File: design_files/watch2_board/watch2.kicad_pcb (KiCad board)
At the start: 16 copper layers, 43.7 x 35.6 mm, 8 parts, among them U1 ESP32-WROVER

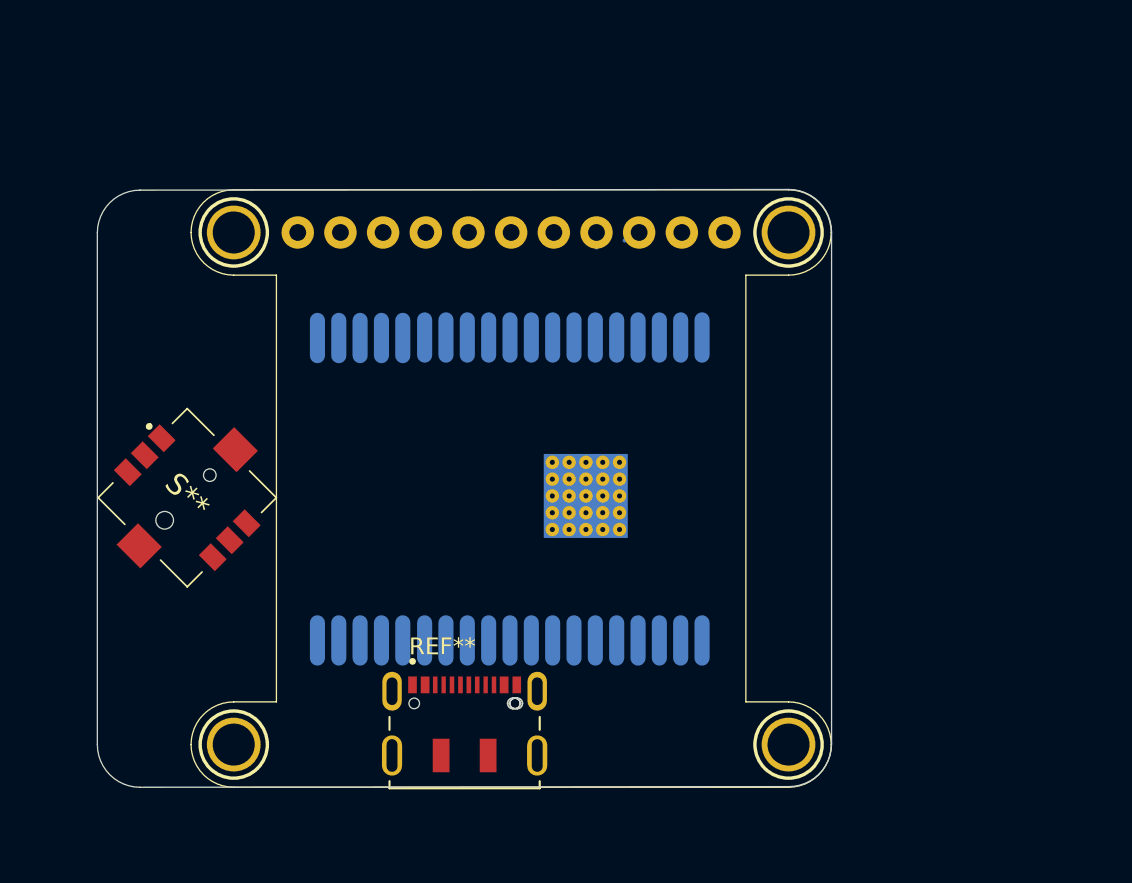
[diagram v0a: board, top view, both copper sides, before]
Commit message: added torch + ir stuff to schematic and did some pcb stuff
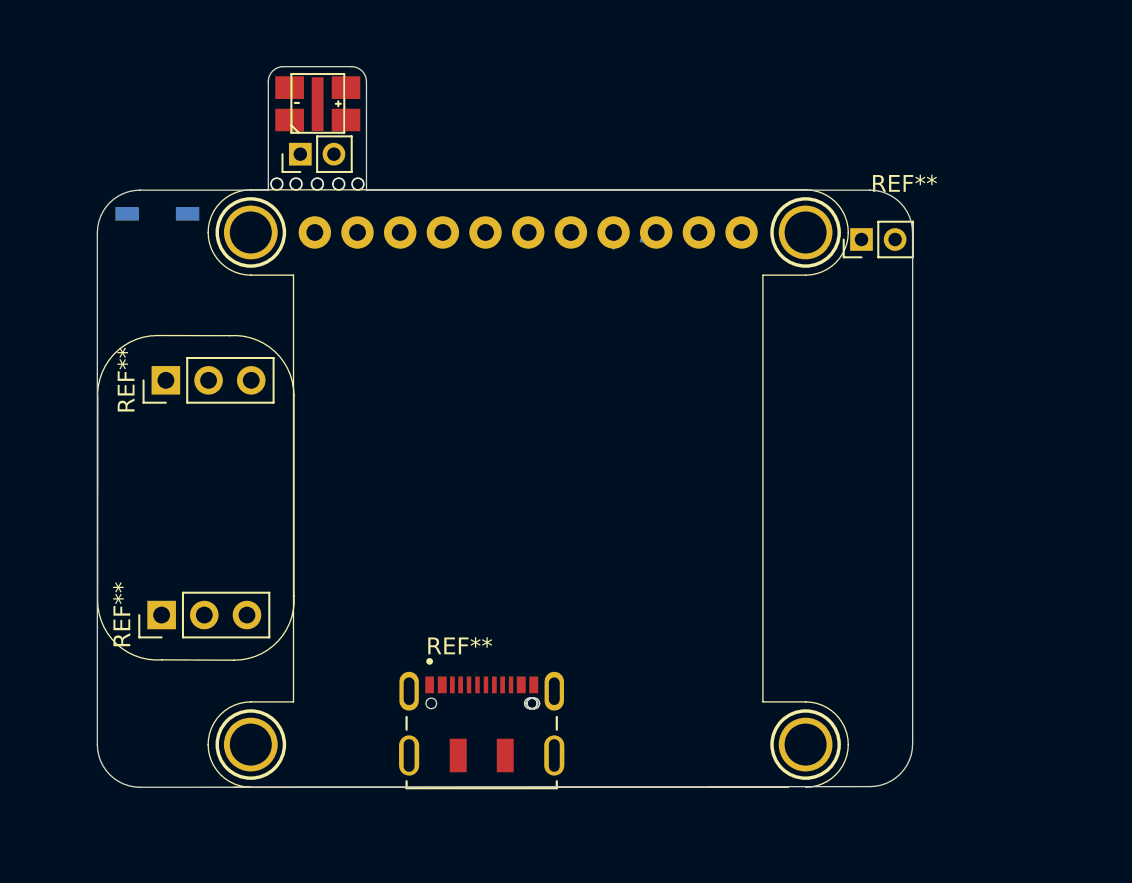
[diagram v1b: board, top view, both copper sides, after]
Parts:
- removed S**: SKRHABE010, Alice's Library:SKRHABE010
- removed U1: ESP32-WROVER, Alice's Library:ESP32-WROVER
- added IR LED: SOD4223X290N, Alice's Library:SOD4223X290N, B.Cu at (131.6, 86.6)
- added REF**: PinHeader_1x03_P2.54mm_Vertical, Connector_PinHeader_2.54mm:PinHeader_1x03_P2.54mm_Vertical, F.Cu at (132.1, 96.5)
- added REF**: PinHeader_1x03_P2.54mm_Vertical, Connector_PinHeader_2.54mm:PinHeader_1x03_P2.54mm_Vertical, F.Cu at (131.8, 110.5)
- added REF**: PinHeader_1x02_P2.00mm_Vertical, Connector_PinHeader_2.00mm:PinHeader_1x02_P2.00mm_Vertical, F.Cu at (140.1, 83.1)
- added REF**: PinHeader_1x02_P2.00mm_Vertical, Connector_PinHeader_2.00mm:PinHeader_1x02_P2.00mm_Vertical, F.Cu at (173.5, 88.1)
- added REF**: MLCAWT-A1-0000-000XE1, Alice's Library:MLCAWT-A1-0000-000XE1, F.Cu at (141.1, 80.1)
- moved U$7 1.02 mm to (137.1, 118.2)
- moved U$9 1.02 mm to (137.1, 87.7)
- moved JP1 1.02 mm to (153.6, 87.7)
- moved REF** 1.02 mm to (150.9, 115.7)
- moved U$10 1.02 mm to (170.2, 87.7)
- moved U$8 1.02 mm to (170.2, 118.2)
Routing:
- net (no net): vias 0 -> 5
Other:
- board size 43.7 x 35.6 mm -> 48.5 x 42.9 mm

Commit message: created watch2 pcb it's mostly populated and wired up.  i haven't checked it yet, and i haven't figured out how to make IO0 externaly pressable yet :)
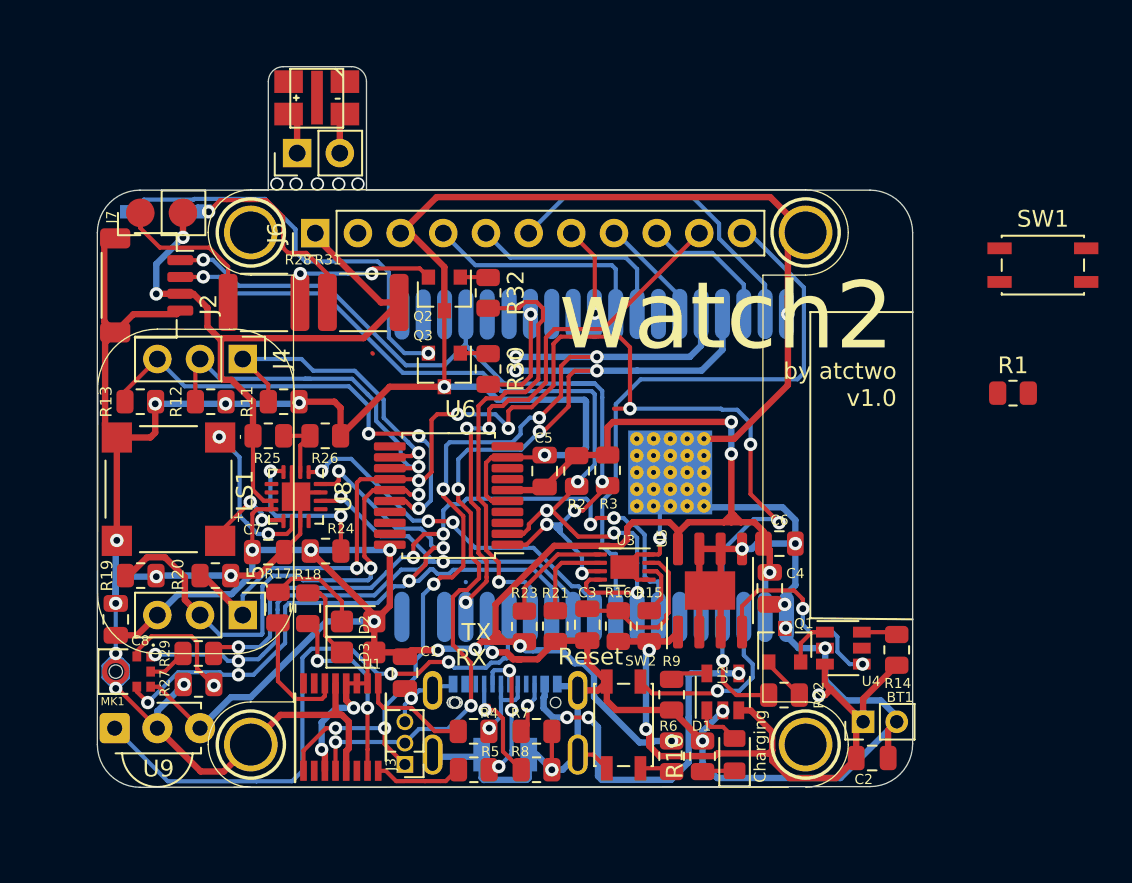
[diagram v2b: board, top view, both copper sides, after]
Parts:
- removed IR LED: SOD4223X290N, Alice's Library:SOD4223X290N
- removed JP1: , 1X11_ROUND_76
- removed REF** (x2): PinHeader_1x03_P2.54mm_Vertical, Connector_PinHeader_2.54mm:PinHeader_1x03_P2.54mm_Vertical
- removed REF** (x2): PinHeader_1x02_P2.00mm_Vertical, Connector_PinHeader_2.00mm:PinHeader_1x02_P2.00mm_Vertical
- removed REF**: MLCAWT-A1-0000-000XE1, Alice's Library:MLCAWT-A1-0000-000XE1
- removed REF**: JAE_DX07S016JA1R1500, Alice's Library:JAE_DX07S016JA1R1500
- added BT1: Battery_Cell, Connector_PinHeader_2.00mm:PinHeader_1x02_P2.00mm_Vertical, F.Cu at (173.6, 116.8)
- added C1: 0.1uF, Capacitor_SMD:C_0805_2012Metric, F.Cu at (146.3, 113.9)
- added C2: 10uF, Capacitor_SMD:C_0805_2012Metric, F.Cu at (174.1, 119.0)
- added C3: 10nF, Capacitor_SMD:C_0805_2012Metric, F.Cu at (157.2, 111.1)
- added C4: 10uF, Capacitor_SMD:C_0805_2012Metric, F.Cu at (168.0, 108.9)
- added C5: 0.1uF, Capacitor_SMD:C_0805_2012Metric, F.Cu at (154.6, 101.9)
- added C6: 0.1uF, Capacitor_SMD:C_0805_2012Metric, F.Cu at (168.6, 106.2)
- added C7: 0.1uF, Capacitor_SMD:C_0805_2012Metric, F.Cu at (138.2, 106.7)
- added C8: 0.1uF, Capacitor_SMD:C_0805_2012Metric, F.Cu at (129.1, 110.7)
- added D1: LED, LED_SMD:LED_0805_2012Metric_Castellated, F.Cu at (165.9, 118.8)
- added D2: TX, LED_SMD:LED_0805_2012Metric_Castellated, F.Cu at (143.5, 110.9)
- added D3: RX, LED_SMD:LED_0805_2012Metric_Castellated, F.Cu at (143.5, 112.7)
- added D4: LED_TORCH, Alice's Library:MLCAWT-A1-0000-000XE1, F.Cu at (141.1, 79.7)
- added D5: LED_IR, Alice's Library:SOD4223X290N, B.Cu at (131.8, 86.5)
- added J1: USB_C_Receptacle_USB2.0, Alice's Library:JAE_DX07S016JA1R1500, B.Cu at (152.3, 115.7)
- added J2: STEMMA QT, Connector_JST:JST_SH_SM04B-SRSS-TB_1x04-1MP_P1.00mm_Horizontal, F.Cu at (130.9, 90.9)
- added J3: UART Connector, Connector_PinHeader_1.27mm:PinHeader_1x03_P1.27mm_Vertical, F.Cu at (146.3, 119.4)
- added J4: Conn_01x03_Male, Connector_PinHeader_2.54mm:PinHeader_1x03_P2.54mm_Vertical, F.Cu at (136.7, 95.2)
- added J5: Conn_01x03_Male, Connector_PinHeader_2.54mm:PinHeader_1x03_P2.54mm_Vertical, F.Cu at (136.7, 110.5)
- added J6: TFT Connector, Connector_PinHeader_2.54mm:PinHeader_1x11_P2.54mm_Vertical, F.Cu at (141.0, 87.8)
- added J7: Torch Connector (main board), Connector_PinHeader_2.54mm:PinHeader_1x02_P2.54mm_Vertical, F.Cu at (130.6, 86.6)
- added J8: Torch Connector (daughter board), Connector_PinHeader_2.54mm:PinHeader_1x02_P2.54mm_Vertical, F.Cu at (139.9, 83.0)
- added LS1: Speaker, Alice's Library:XDCR_CMT-7525-80-SMT-TR, F.Cu at (132.2, 103.0)
- added MK1: SPH0645LM4H-B, Alice's Library:MIC_SPH0645LM4H-B, F.Cu at (129.1, 113.9)
- added Q1: Q_NPN_BCE, Package_TO_SOT_SMD:SOT-23, F.Cu at (168.9, 112.3)
- added Q2: Q_NPN_BCE, Package_TO_SOT_SMD:SOT-23, F.Cu at (148.7, 91.4)
- added Q3: Q_NPN_BCE, Package_TO_SOT_SMD:SOT-23, F.Cu at (148.7, 95.9)
- added R1: 1k, Resistor_SMD:R_0805_2012Metric, F.Cu at (182.5, 97.3)
- added R10: 1k, Resistor_SMD:R_0805_2012Metric, F.Cu at (164.0, 118.9)
- added R11: R, Resistor_SMD:R_0805_2012Metric, F.Cu at (139.1, 97.8)
- added R12: R, Resistor_SMD:R_0805_2012Metric, F.Cu at (134.7, 97.8)
- added R13: R, Resistor_SMD:R_0805_2012Metric, F.Cu at (130.6, 97.8)
- added R14: 1k, Resistor_SMD:R_0805_2012Metric, F.Cu at (175.6, 112.6)
- added R15: 1k, Resistor_SMD:R_0805_2012Metric, F.Cu at (160.8, 111.1)
- added R16: 180R, Resistor_SMD:R_0805_2012Metric, F.Cu at (159.0, 111.1)
- added R17: 1k, Resistor_SMD:R_0805_2012Metric, F.Cu at (138.7, 110.0)
- added R18: 1k, Resistor_SMD:R_0805_2012Metric, F.Cu at (140.5, 110.1)
- added R19: R, Resistor_SMD:R_0805_2012Metric, F.Cu at (130.6, 108.1)
- added R2: 4k7, Resistor_SMD:R_0805_2012Metric, F.Cu at (156.5, 101.9)
- added R20: R, Resistor_SMD:R_0805_2012Metric, F.Cu at (135.0, 108.1)
- added R21: 4k1, Resistor_SMD:R_0805_2012Metric, F.Cu at (155.3, 111.1)
- added R22: 1k, Resistor_SMD:R_0805_2012Metric, F.Cu at (168.9, 115.3)
- added R23: 4k7, Resistor_SMD:R_0805_2012Metric, F.Cu at (153.4, 111.2)
- added R24: 680k, Resistor_SMD:R_0805_2012Metric, F.Cu at (141.6, 106.7)
- added R25: 100k, Resistor_SMD:R_0805_2012Metric, F.Cu at (138.2, 99.8)
- added R26: 100k, Resistor_SMD:R_0805_2012Metric, F.Cu at (141.6, 99.8)
- added R27: 10k, Resistor_SMD:R_0805_2012Metric, F.Cu at (134.0, 114.6)
- added R28: 100R, Resistor_SMD:R_1812_4532Metric, F.Cu at (137.9, 91.9)
- added R29: 68R, Resistor_SMD:R_0805_2012Metric, F.Cu at (134.0, 112.8)
- added R3: 4k7, Resistor_SMD:R_0805_2012Metric, F.Cu at (158.4, 101.9)
- added R30: 1k, Resistor_SMD:R_0805_2012Metric, F.Cu at (151.3, 95.8)
- added R31: 100R, Resistor_SMD:R_1812_4532Metric, F.Cu at (143.8, 91.9)
- added R32: 1k, Resistor_SMD:R_0805_2012Metric, F.Cu at (151.3, 91.3)
- added R4: 27R, Resistor_SMD:R_0805_2012Metric, F.Cu at (150.4, 117.4)
- added R5: 27R, Resistor_SMD:R_0805_2012Metric, F.Cu at (150.4, 119.7)
- added R6: 1k, Resistor_SMD:R_0805_2012Metric, F.Cu at (162.2, 118.9)
- added R7: 5k1, Resistor_SMD:R_0805_2012Metric, F.Cu at (154.1, 117.4)
- added R8: 5k1, Resistor_SMD:R_0805_2012Metric, F.Cu at (154.1, 119.7)
- added R9: 2k, Resistor_SMD:R_0805_2012Metric, F.Cu at (162.2, 115.2)
- added SW1: SW_Push, Button_Switch_SMD:SW_SPST_EVQP2, F.Cu at (184.3, 89.7)
- added SW2: SW_Push, Button_Switch_SMD:SW_SPST_EVQP2, F.Cu at (159.3, 117.0)
- added U1: FT230XS, Package_SO:SSOP-16_3.9x4.9mm_P0.635mm, F.Cu at (142.5, 117.2)
- added U2: MCP73831-2-OT, Package_TO_SOT_SMD:SOT-23-5, F.Cu at (165.2, 115.1)
- added U3: MAX17043G+U, Package_DFN_QFN:DFN-8-1EP_3x2mm_P0.5mm_EP1.7x1.4mm, F.Cu at (159.4, 107.6)
- added U4: MAX16150AUT+T, Package_TO_SOT_SMD:SOT-23-6, F.Cu at (172.4, 112.5)
- added U5: MAX604, Package_SO:SOIC-8-1EP_3.9x4.9mm_P1.27mm_EP2.29x3mm, F.Cu at (164.5, 109.0)
- added U6: MCP23008-xSS, Package_SO:SSOP-20_5.3x7.2mm_P0.65mm, F.Cu at (148.9, 103.4)
- added U7: ESP32-WROVER, Alice's Library:ESP32-WROVER, B.Cu at (169.9, 101.6)
- added U8: MAX98357AETE+T, Package_DFN_QFN:QFN-16-1EP_3x3mm_P0.5mm_EP1.7x1.7mm, F.Cu at (139.8, 103.4)
- added U9: TSOP38238, OptoDevice:Vishay_MINICAST-3Pin, F.Cu at (129.0, 117.2)
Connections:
- U$10 pad P$1: (no net) -> GND
- U$7 pad P$1: (no net) -> GND
- U$8 pad P$1: (no net) -> GND
- U$9 pad P$1: (no net) -> GND
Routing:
- net GND: track 0.00 -> 296.1 mm, vias 0 -> 24
- net +3V3: track 0.00 -> 182.4 mm, vias 0 -> 15
- net DPAD_ENTER: track 0.00 -> 76.3 mm, vias 0 -> 8
- net +5V: track 0.00 -> 61.4 mm, vias 0 -> 6
- net ESP_RX: track 0.00 -> 54.6 mm, vias 0 -> 7
- net I2C_SDA: track 0.00 -> 54.0 mm, vias 0 -> 5
- net ESP_TX: track 0.00 -> 53.7 mm, vias 0 -> 6
- net I2C_SCL: track 0.00 -> 53.2 mm, vias 0 -> 5
- net I2S_BLK: track 0.00 -> 45.5 mm, vias 0 -> 5
- net I2S_LRC: track 0.00 -> 39.7 mm, vias 0 -> 4
- net I2S_DIN: track 0.00 -> 39.5 mm, vias 0 -> 5
- net IR_RECV: track 0.00 -> 36.9 mm, vias 0 -> 2
- net TFT_BL: track 0.00 -> 35.8 mm
- net SD_CS: track 0.00 -> 32.4 mm, vias 0 -> 3
- net DPAD_DOWN: track 0.00 -> 30.2 mm, vias 0 -> 2
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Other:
- board text added: "+"
- board text added: "-"
- board text added: "Charging"
- board text added: "RX"
- board text added: "Reset"
- board text added: "Serial Number"
- board text added: "TX"
- board text added: "by atctwo v1.0"
- board text added: "watch2"

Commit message: created initial version of the pcb
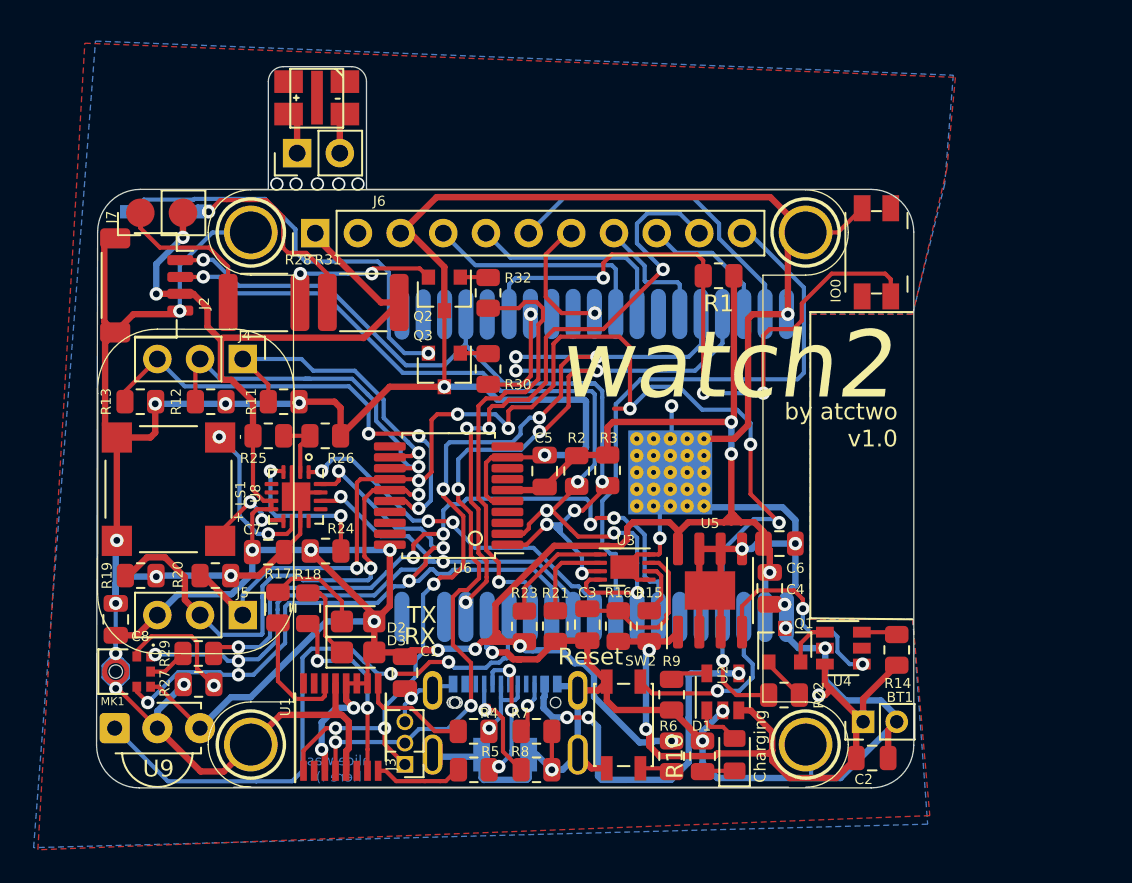
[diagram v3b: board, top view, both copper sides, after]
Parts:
- removed SW1: SW_Push, Button_Switch_SMD:SW_SPST_EVQP2
- added IO0: Panasonic_EVQPUJ_EVQPUA, Button_Switch_SMD:Panasonic_EVQPUJ_EVQPUA, F.Cu at (174.4, 88.9)
- moved R1 18.9 mm to (165.0, 90.3), turned to 180 degrees
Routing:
- net ESP_IO0: track 0.00 -> 40.5 mm, vias 0 -> 3
- net GND: track 296.1 -> 314.7 mm, vias 24 -> 26
- net +3V3: track 182.4 -> 191.1 mm
- net SD_CS: track 32.4 -> 37.2 mm, vias 3 -> 4
- net TFT_CS: track 5.34 -> 7.91 mm
- net Net-(J7-Pad1): track 19.6 -> 21.3 mm
- net DPAD_ENTER: track 76.3 -> 77.3 mm
- net TFT_RESET: track 6.52 -> 7.53 mm
- net USB_D+: track 8.66 -> 9.31 mm
- net +5V: track 61.4 -> 62.0 mm
- added copper zone on B.Cu, net GND
- added copper zone on F.Cu, net GND
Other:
- board size 48.5 x 42.9 mm -> 48.6 x 42.9 mm
- copper layers 16 -> 2
- board text added: "alice was here :)"

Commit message: added pcb v2 files again
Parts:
- removed D4: LED_TORCH, Alice's Library:MLCAWT-A1-0000-000XE1
- removed J8: Torch Connector (daughter board), Connector_PinHeader_2.54mm:PinHeader_1x02_P2.54mm_Vertical
- removed Q1: Q_NPN_BCE, Package_TO_SOT_SMD:SOT-23
- removed R16: 180R, Resistor_SMD:R_0805_2012Metric
- removed R21: 4k1, Resistor_SMD:R_0805_2012Metric
- removed R22: 1k, Resistor_SMD:R_0805_2012Metric
- removed R23: 4k7, Resistor_SMD:R_0805_2012Metric
- added ?: , label, F.Cu at (147.4, 111.2)
- added ?: , label, F.Cu at (147.4, 109.4)
- added ?: , label, F.Cu at (164.9, 96.2)
- added ?: , label, B.Cu at (138.6, 102.8)
- added BLK: TestPoint_Pad_D1.0mm, TestPoint:TestPoint_Pad_D1.0mm, F.Cu at (137.6, 115.3)
- added C9: 0.1uF, Capacitor_SMD:C_0805_2012Metric, F.Cu at (144.7, 98.1)
- added D+: TestPoint_Pad_D1.0mm, TestPoint:TestPoint_Pad_D1.0mm, F.Cu at (153.3, 114.6)
- added D-: TestPoint_Pad_D1.0mm, TestPoint:TestPoint_Pad_D1.0mm, F.Cu at (151.9, 114.6)
- added DIN: TestPoint_Pad_D1.0mm, TestPoint:TestPoint_Pad_D1.0mm, F.Cu at (137.6, 112.5)
- added DOUT: TestPoint_Pad_D1.0mm, TestPoint:TestPoint_Pad_D1.0mm, F.Cu at (143.5, 101.4)
- added LRC: TestPoint_Pad_D1.0mm, TestPoint:TestPoint_Pad_D1.0mm, F.Cu at (137.6, 113.9)
- added REF**: PinHeader_1x01_P2.54mm_Vertical, Connector_PinHeader_2.54mm:PinHeader_1x01_P2.54mm_Vertical, F.Cu at (171.3, 91.3)
- added REF**: PinHeader_1x03_P2.54mm_Vertical, Connector_PinHeader_2.54mm:PinHeader_1x03_P2.54mm_Vertical, F.Cu at (173.8, 91.3)
- added SW2: SW_Push, Button_Switch_SMD:SW_SPST_EVQP2, B.Cu at (159.3, 117.0)
- added SW3: Power Button, Button_Switch_SMD:SW_SPST_EVQP2, B.Cu at (172.3, 114.2)
- added Speaker: PinHeader_1x02_P2.54mm_Vertical, Connector_PinHeader_2.54mm:PinHeader_1x02_P2.54mm_Vertical, F.Cu at (132.8, 101.6)
- added U10: MCP9808_MSOP, Package_SO:MSOP-8_3x3mm_P0.65mm, F.Cu at (143.6, 95.6)
- C3: value 10nF -> 0.1uF
- IO0: moved to B.Cu
- J6: footprint Connector_PinHeader_2.54mm:PinHeader_1x11_P2.54mm_Vertical -> Connector_PinSocket_2.54mm:PinSocket_1x11_P2.54mm_Vertical
- R15: value 1k -> 10k
- R28, R31: footprint Resistor_SMD:R_1812_4532Metric -> Resistor_SMD:R_1210_3225Metric
- R30, R32: value 1k -> 330R
- U3: value MAX17043G+U -> LC709203FQH-01TWG; footprint Package_DFN_QFN:DFN-8-1EP_3x2mm_P0.5mm_EP1.7x1.4mm -> Package_DFN_QFN:WDFN-8-1EP_4x3mm_P0.65mm_EP2.4x1.8mm
- moved IO0 46.7 mm to (129.8, 102.8), turned to 90 degrees
- moved J6 25.4 mm to (166.4, 87.8), turned to 270 degrees
- moved D3 1.46 mm to (143.5, 111.3)
- moved D2 1.46 mm to (143.5, 109.4)
- moved Q3 1.19 mm to (148.4, 94.7)
- moved U3 0.90 mm to (158.5, 107.9)
- moved R15 0.87 mm to (160.0, 110.9), turned to 0 degrees
- moved C3 0.54 mm to (156.7, 110.9), turned to 180 degrees
- moved R31 0.51 mm to (144.3, 91.9)
- moved Q2 0.23 mm to (148.5, 91.2)
- moved D1 0.16 mm to (166.0, 118.9), turned to 270 degrees
- moved R10 0.06 mm to (164.1, 118.9)
- moved R28 0.06 mm to (137.9, 91.9)
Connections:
- C3 pad 1: Net-(C3-Pad1) -> +5V
- J1 pad 1: GND -> (no net)
- J1 pad 11: +5V -> (no net)
- J1 pad 12: GND -> (no net)
- J1 pad 2: +5V -> (no net)
- J1 pad 3 (CC1): Net-(J1-PadA5) -> (no net)
- J1 pad 7: USB_D- -> USB_D+
- J1 pad 8: USB_D+ -> USB_D-
- J1 pad 9 (CC2): Net-(J1-PadB5) -> (no net)
- J1 pad S2: GND -> (no net)
- J1 pad S3: GND -> (no net)
- J1 pad S5: GND -> (no net)
- J1 pad S6: GND -> (no net)
- J2 pad 1: I2C_SCL -> GND
- J2 pad 2: I2C_SDA -> +3V3
- J2 pad 3: +3V3 -> I2C_SDA
- J2 pad 4: GND -> I2C_SCL
- LS1 pad 1: GND -> Net-(LS1-Pad1)
- LS1 pad 2: GND -> Net-(LS1-Pad2)
- Q2 pad 2: Net-(J7-Pad1) -> GND
- Q2 pad 3: GND -> Net-(Q2-Pad3)
- Q3 pad 2: Net-(D5-Pad1) -> GND
- Q3 pad 3: GND -> Net-(D5-Pad1)
- R10 pad 1: Net-(D1-Pad1) -> Net-(D1-Pad2)
- R10 pad 2: GND -> Net-(J1-PadA4)
- R15 pad 1: Net-(R15-Pad1) -> +5V
- R15 pad 2: +5V -> Net-(R15-Pad2)
- R28 pad 2: Net-(J7-Pad1) -> Net-(Q2-Pad3)
- U2 pad 1: Net-(D1-Pad2) -> Net-(D1-Pad1)
- U2 pad 4: +5V -> Net-(J1-PadA4)
- U3 pad 2: Net-(R15-Pad1) -> GND
- U3 pad 3: Net-(C3-Pad1) -> +5V
- U3 pad 4: GND -> Net-(R15-Pad2)
- U3 pad 7: I2C_SCL -> I2C_SDA
- U3 pad 8: I2C_SDA -> I2C_SCL
- U5 pad 9: GND -> (no net)
- U6 pad 3: Net-(U6-Pad3) -> GND
- U6 pad 4: Net-(U6-Pad4) -> GND
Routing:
- net ESP_IO0: track 40.5 -> 80.8 mm, vias 3 -> 5
- net ESP_RX: track 54.6 -> 87.8 mm, vias 7 -> 9
- net TFT_DC: track 8.59 -> 31.8 mm, vias 0 -> 1
- net TFT_BL: track 35.8 -> 55.5 mm, vias 0 -> 1
- net SD_CS: track 37.2 -> 55.9 mm, vias 4 -> 5
- net TFT_RESET: track 7.53 -> 23.9 mm
- net +3V3: track 191.1 -> 206.5 mm, vias 15 -> 16
- net Net-(Q2-Pad3): track 0.00 -> 13.5 mm, vias 0 -> 2
- net +5V: track 62.0 -> 75.0 mm
- net GND: track 314.7 -> 326.4 mm, vias 26 -> 29
- net Net-(J7-Pad1): track 21.3 -> 9.64 mm, vias 2 -> 0
- net Net-(C3-Pad1): track 9.61 -> 0.00 mm
- net DPAD_ENTER: track 77.3 -> 69.4 mm, vias 8 -> 7
- net TFT_CLOCK: track 14.5 -> 6.59 mm
- net Net-(U3-Pad5): track 6.73 -> 0.00 mm
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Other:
- board size 48.6 x 42.9 mm -> 48.6 x 35.6 mm
- board text added: "3v3"
- board text added: "GND"
- board text added: "Power"
- board text added: "SCL"
- board text added: "SDA"
- board text added: "STEMMA QT"
- board text added: "by atctwo v1.1"
- board text removed: "Serial Number"
- board text removed: "by atctwo v1.0"
- board text removed: "watch2"
